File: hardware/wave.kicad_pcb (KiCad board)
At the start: 4 copper layers, 60 x 60 mm, 123 parts, among them J101 WAGO 2065-100, J102 WAGO 2065-100, J103 Cortex, J104 WAGO 2065-100, J105 WAGO 2065-100, J106 WAGO 2065-100, J107 WAGO 2065-100, J301 2x05_Horizontal, J401 2x05_Horizontal, J501 WAGO 2065-100, J502 WAGO 2065-100, Q201 IRF9358, SW101 SKSG, SW102 SKSG, U101 ATSAMD51J, U102 TPS78433QWDRBRQ1, U201 MA12070P, U301 THVD2442, U401 THVD2442, U501 74AHC1G125, Y101 32k768

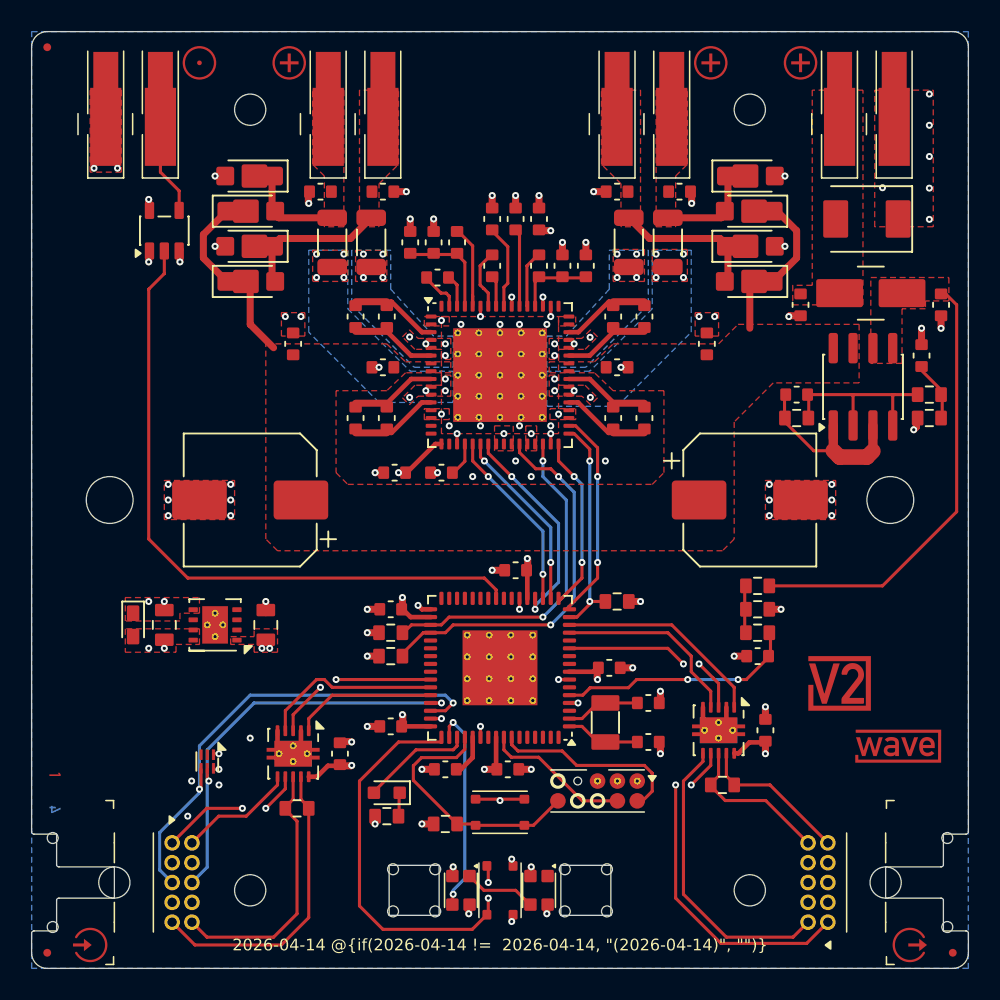
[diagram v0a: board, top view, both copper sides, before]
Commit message: Update power routing
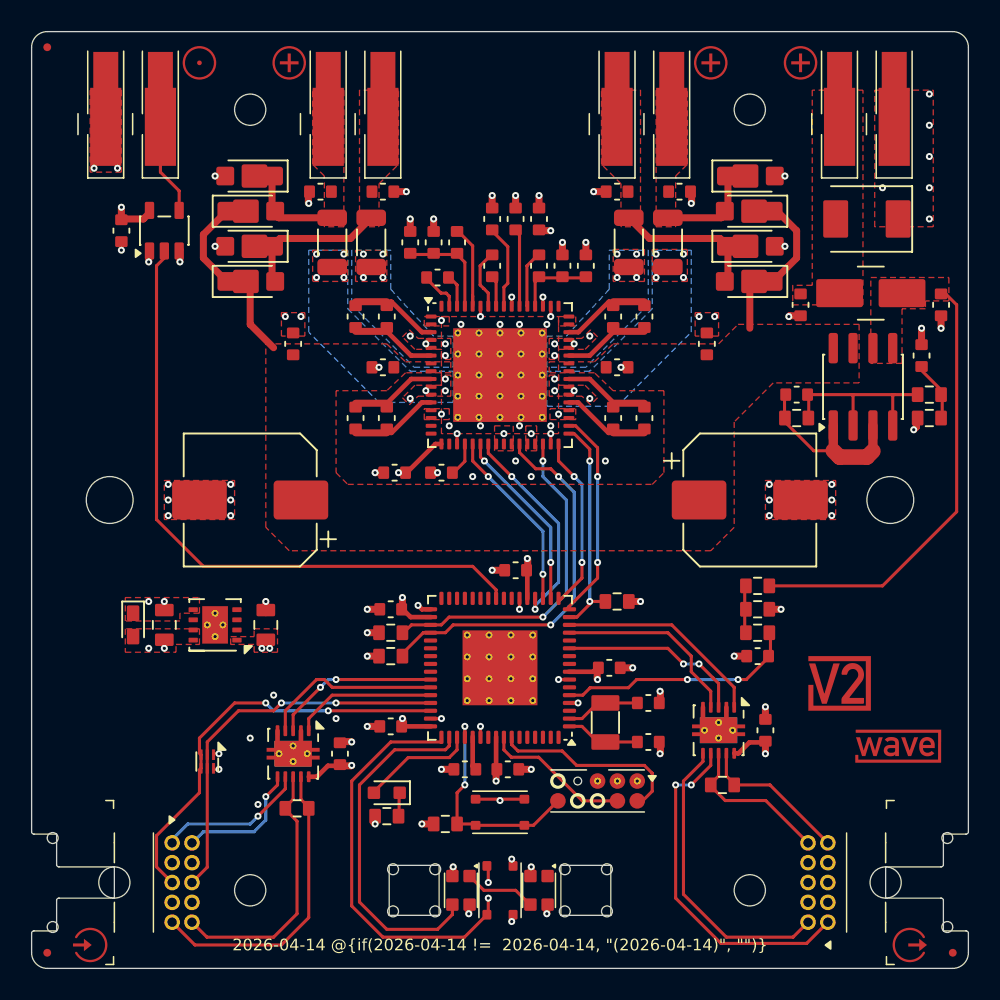
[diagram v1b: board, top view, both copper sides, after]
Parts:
- added C501: 0u1, V2_Capacitor_SMD:C_1608, F.Cu at (72.8, 67.8)
- C101, C102, C103, C104, C105, C106, C107, C108, C109, C110, C111, C201, C202, C203, C204, C205, C206, C207, C208, C209, C210, C211, C212, C213, C214, C215, C216, C217, C219, C220, C221, C222, C223, C224, C225, C226, C227, C228, C229, C230, C231, C232, C301, C401: footprint V2_Capacitor_SMD:C_0603 -> V2_Capacitor_SMD:C_1608
- C112, C113: footprint V2_Capacitor_SMD:C_0805 -> V2_Capacitor_SMD:C_2012
- D101: footprint V2_LED:LED_0603 -> V2_LED:LED_1608
- INFO102: value Layer_Numbers -> Layer_Numbers-4; footprint V2_Production:Layer_Numbers -> V2_Production:Layer_Numbers-4
- R101, R102, R103, R104, R105, R106, R107, R108, R201, R202, R203, R301, R401: footprint V2_Resistor_SMD:R_0603 -> V2_Resistor_SMD:R_1608
- TVS102: footprint V2_Diode_SMD:D_0603 -> V2_Diode_SMD:D_1608
- moved C104 1.25 mm to (94.8, 102.2)
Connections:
- ESD101 pad 2: unconnected-(ESD101-D2-Pad2) -> /USB-
- ESD101 pad 3: unconnected-(ESD101-D1-Pad3) -> /USB+
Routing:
- net /LED-Button: track 13.3 -> 22.5 mm, vias 2 -> 0
- net /USB+: track 30.9 -> 26.9 mm
- net /RESET: track 16.6 -> 14.3 mm, vias 0 -> 2
- net /USB-: track 26.7 -> 24.8 mm
- net +5V: track 8.63 -> 10.5 mm
- net /LED-Data: track 43.2 -> 41.8 mm
- net /Button: track 27.0 -> 28.4 mm
- net /Link Plug/TX-Y: track 7.54 -> 8.42 mm, vias 0 -> 1
- net /Link Plug/TX-Z: track 9.46 -> 9.58 mm, vias 2 -> 1
- net GND: vias 100 -> 101
- removed copper zone on In2.Cu, net +3V3
- removed copper zone on In2.Cu, net +5V
- removed copper zone on B.Cu, net GND

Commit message: Update stackup
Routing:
- net +5V: track 10.5 -> 132.5 mm, vias 11 -> 12
- net +3V3: track 22.7 -> 110.5 mm, vias 14 -> 15
- net GND: track 46.0 -> 43.6 mm, vias 101 -> 92
- net /LED-Data: track 41.8 -> 42.5 mm
- net /Link Socket/TX-Z: track 22.3 -> 21.7 mm
- added copper zone on B.Cu, net +5V
